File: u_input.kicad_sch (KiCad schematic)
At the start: 21 parts, among them U1 ${SIM.PARAMS}, U2 ${SIM.PARAMS}, U3 ${SIM.PARAMS}, U4 ${SIM.PARAMS}, U5 ${SIM.PARAMS}, U6 ${SIM.PARAMS}, U7 ${SIM.PARAMS}

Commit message: Before 10K resistors change
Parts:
- R1, R10, R11, R12, R13, R14, R2, R3, R4, R5, R6, R7, R8, R9: footprint (none) -> Resistor_SMD:R_1206_3216Metric_Pad1.30x1.75mm_HandSolder
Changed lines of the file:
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@@
 			)
 		)
-		(property "Footprint" ""
+		(property "Footprint" "Resistor_SMD:R_1206_3216Metric_Pad1.30x1.75mm_HandSolder"
 			(at 71.12 156.972 90)
 			(effects
@@
 			)
 		)
-		(property "Footprint" ""
+		(property "Footprint" "Resistor_SMD:R_1206_3216Metric_Pad1.30x1.75mm_HandSolder"
 			(at 73.66 355.092 90)
 			(effects
@@
 			)
 		)
-		(property "Footprint" ""
+		(property "Footprint" "Resistor_SMD:R_1206_3216Metric_Pad1.30x1.75mm_HandSolder"
 			(at 88.9 336.042 90)
 			(effects
@@
 			)
 		)
-		(property "Footprint" ""
+		(property "Footprint" "Resistor_SMD:R_1206_3216Metric_Pad1.30x1.75mm_HandSolder"
 			(at 71.12 70.612 90)
 			(effects
@@
 			)
 		)
-		(property "Footprint" ""
+		(property "Footprint" "Resistor_SMD:R_1206_3216Metric_Pad1.30x1.75mm_HandSolder"
 			(at 86.36 51.562 90)
 			(effects
@@
 			)
 		)
-		(property "Footprint" ""
+		(property "Footprint" "Resistor_SMD:R_1206_3216Metric_Pad1.30x1.75mm_HandSolder"
 			(at 86.36 137.922 90)
 			(effects
@@
 			)
 		)
-		(property "Footprint" ""
+		(property "Footprint" "Resistor_SMD:R_1206_3216Metric_Pad1.30x1.75mm_HandSolder"
 			(at 71.12 113.792 90)
 			(effects
@@
 			)
 		)
-		(property "Footprint" ""
+		(property "Footprint" "Resistor_SMD:R_1206_3216Metric_Pad1.30x1.75mm_HandSolder"
 			(at 88.9 290.322 90)
 			(effects
@@
 			)
 		)
-		(property "Footprint" ""
+		(property "Footprint" "Resistor_SMD:R_1206_3216Metric_Pad1.30x1.75mm_HandSolder"
 			(at 88.9 247.142 90)
 			(effects
@@
 			)
 		)
-		(property "Footprint" ""
+		(property "Footprint" "Resistor_SMD:R_1206_3216Metric_Pad1.30x1.75mm_HandSolder"
 			(at 88.9 203.962 90)
 			(effects
@@
 			)
 		)
-		(property "Footprint" ""
+		(property "Footprint" "Resistor_SMD:R_1206_3216Metric_Pad1.30x1.75mm_HandSolder"
 			(at 73.66 266.192 90)
 			(effects
@@
 			)
 		)
-		(property "Footprint" ""
+		(property "Footprint" "Resistor_SMD:R_1206_3216Metric_Pad1.30x1.75mm_HandSolder"
 			(at 86.36 94.742 90)
 			(effects
@@
 			)
 		)
-		(property "Footprint" ""
+		(property "Footprint" "Resistor_SMD:R_1206_3216Metric_Pad1.30x1.75mm_HandSolder"
 			(at 73.66 223.012 90)
 			(effects
@@
 			)
 		)
-		(property "Footprint" ""
+		(property "Footprint" "Resistor_SMD:R_1206_3216Metric_Pad1.30x1.75mm_HandSolder"
 			(at 73.66 309.372 90)
 			(effects

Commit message: Before capcitor update
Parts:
- R1, R10, R11, R12, R13, R14, R2, R3, R4, R5, R6, R7, R8, R9: value R -> 10k
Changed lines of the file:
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@@
 			)
 		)
-		(property "Value" "R"
+		(property "Value" "10k"
 			(at 71.12 154.94 90)
 			(effects
@@
 			)
 		)
-		(property "Value" "R"
+		(property "Value" "10k"
 			(at 73.66 353.06 90)
 			(effects
@@
 			)
 		)
-		(property "Value" "R"
+		(property "Value" "10k"
 			(at 88.9 334.01 90)
 			(effects
@@
 			)
 		)
-		(property "Value" "R"
+		(property "Value" "10k"
 			(at 71.12 68.58 90)
 			(effects
@@
 			)
 		)
-		(property "Value" "R"
+		(property "Value" "10k"
 			(at 86.36 49.53 90)
 			(effects
@@
 			)
 		)
-		(property "Value" "R"
+		(property "Value" "10k"
 			(at 86.36 135.89 90)
 			(effects
@@
 			)
 		)
-		(property "Value" "R"
+		(property "Value" "10k"
 			(at 71.12 111.76 90)
 			(effects
@@
 			)
 		)
-		(property "Value" "R"
+		(property "Value" "10k"
 			(at 88.9 288.29 90)
 			(effects
@@
 			)
 		)
-		(property "Value" "R"
+		(property "Value" "10k"
 			(at 88.9 245.11 90)
 			(effects
@@
 			)
 		)
-		(property "Value" "R"
+		(property "Value" "10k"
 			(at 88.9 201.93 90)
 			(effects
@@
 			)
 		)
-		(property "Value" "R"
+		(property "Value" "10k"
 			(at 73.66 264.16 90)
 			(effects
@@
 			)
 		)
-		(property "Value" "R"
+		(property "Value" "10k"
 			(at 86.36 92.71 90)
 			(effects
@@
 			)
 		)
-		(property "Value" "R"
+		(property "Value" "10k"
 			(at 73.66 220.98 90)
 			(effects
@@
 			)
 		)
-		(property "Value" "R"
+		(property "Value" "10k"
 			(at 73.66 307.34 90)
 			(effects

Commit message: Updated: power
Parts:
- removed U2: ${SIM.PARAMS}, symbol Simulation_SPICE:OPAMP
- added U43: TLV9061xDBV, Package_TO_SOT_SMD:SOT-23-5, symbol Amplifier_Operational:TLV9061xDBV
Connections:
- net -VCC is gone; now on net GND: U1.4 (V-), U3.4 (V-), U4.4 (V-), U5.4 (V-), U6.4 (V-), U7.4 (V-)
- net -Vu1: now also U43.1
- net GND: now also U43.2 (V-), U43.3 (+)
- net VCC: now also U43.5 (V+)
- net at R3.2, R4.1: now also U43.4 (-)

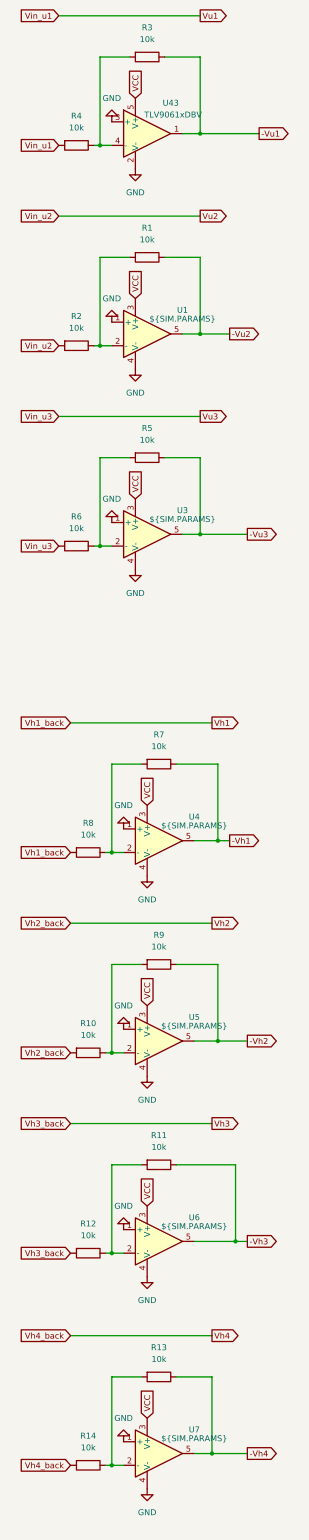
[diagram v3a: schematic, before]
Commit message: Updated: op amps
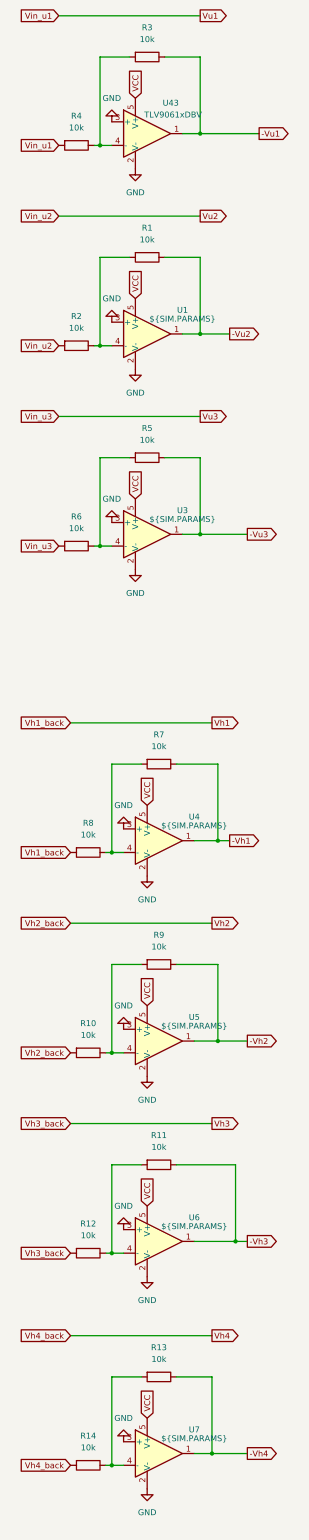
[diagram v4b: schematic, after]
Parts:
- U1, U3, U4, U5, U6, U7: footprint (none) -> Package_TO_SOT_SMD:SOT-23-5; symbol Simulation_SPICE:OPAMP -> Amplifier_Operational:TLV9061xDBV
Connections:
- net -Vh1: now also U4.1; no longer U4.5
- net -Vh2: now also U5.1; no longer U5.5
- net -Vh3: now also U6.1; no longer U6.5
- net -Vh4: now also U7.1; no longer U7.5
- net -Vu2: now also U1.1; no longer U1.5
- net -Vu3: now also U3.1; no longer U3.5
- net GND: now also U1.2 (V-), U1.3 (+), U3.2 (V-), U3.3 (+), U4.2 (V-), U4.3 (+), U5.2 (V-), U5.3 (+), U6.2 (V-), U6.3 (+), U7.2 (V-), U7.3 (+); no longer U1.1 (+), U1.4 (V-), U3.1 (+), U3.4 (V-), U4.1 (+), U4.4 (V-), U5.1 (+), U5.4 (V-), U6.1 (+), U6.4 (V-), U7.1 (+), U7.4 (V-)
- net VCC: now also U1.5 (V+), U3.5 (V+), U4.5 (V+), U5.5 (V+), U6.5 (V+), U7.5 (V+); no longer U1.3 (V+), U3.3 (V+), U4.3 (V+), U5.3 (V+), U6.3 (V+), U7.3 (V+)
- net at R5.2, R6.1: now also U3.4 (-); no longer U3.2 (-)
- net at R13.2, R14.1: now also U7.4 (-); no longer U7.2 (-)
- net at R1.2, R2.1: now also U1.4 (-); no longer U1.2 (-)
- net at R11.2, R12.1: now also U6.4 (-); no longer U6.2 (-)
- net at R10.1, R9.2: now also U5.4 (-); no longer U5.2 (-)
- net at R7.2, R8.1: now also U4.4 (-); no longer U4.2 (-)
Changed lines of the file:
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@@
 	)
 	(symbol
-		(lib_id "Simulation_SPICE:OPAMP")
+		(lib_id "Amplifier_Operational:TLV9061xDBV")
 		(at 86.36 113.03 0)
 		(unit 1)
@@
 			)
 		)
-		(property "Footprint" ""
-			(at 86.36 113.03 0)
-			(effects
-				(font
-					(size 1.27 1.27)
-				)
-				(hide yes)
-			)
-		)
-		(property "Datasheet" "https://ngspice.sourceforge.io/docs/ngspice-html-manual/manual.xhtml#sec__SUBCKT_Subcircuits"
-			(at 86.36 113.03 0)
-			(effects
-				(font
-					(size 1.27 1.27)
-				)
-				(hide yes)
-			)
-		)
-		(property "Description" "Operational amplifier, single"
+		(property "Footprint" "Package_TO_SOT_SMD:SOT-23-5"
+			(at 71.12 132.08 0)
+			(effects
+				(font
+					(size 1.27 1.27)
+				)
+				(justify left)
+				(hide yes)
+			)
+		)
+		(property "Datasheet" "https://www.ti.com/lit/ds/symlink/tlv9061.pdf"
+			(at 86.36 92.71 0)
+			(effects
+				(font
+					(size 1.27 1.27)
+				)
+				(hide yes)
+			)
+		)
+		(property "Description" "10-MHz, RRIO, CMOS Operational Amplifiers for Cost-Sensitive Systems, SOT-23-5"
 			(at 86.36 113.03 0)
 			(effects
@@
 	)
 	(symbol
-		(lib_id "Simulation_SPICE:OPAMP")
+		(lib_id "Amplifier_Operational:TLV9061xDBV")
 		(at 88.9 265.43 0)
 		(unit 1)
@@
 			)
 		)
-		(property "Footprint" ""
-			(at 88.9 265.43 0)
-			(effects
-				(font
-					(size 1.27 1.27)
-				)
-				(hide yes)
-			)
-		)
-		(property "Datasheet" "https://ngspice.sourceforge.io/docs/ngspice-html-manual/manual.xhtml#sec__SUBCKT_Subcircuits"
-			(at 88.9 265.43 0)
-			(effects
-				(font
-					(size 1.27 1.27)
-				)
-				(hide yes)
-			)
-		)
-		(property "Description" "Operational amplifier, single"
+		(property "Footprint" "Package_TO_SOT_SMD:SOT-23-5"
+			(at 73.66 284.48 0)
+			(effects
+				(font
+					(size 1.27 1.27)
+				)
+				(justify left)
+				(hide yes)
+			)
+		)
+		(property "Datasheet" "https://www.ti.com/lit/ds/symlink/tlv9061.pdf"
+			(at 88.9 245.11 0)
+			(effects
+				(font
+					(size 1.27 1.27)
+				)
+				(hide yes)
+			)
+		)
+		(property "Description" "10-MHz, RRIO, CMOS Operational Amplifiers for Cost-Sensitive Systems, SOT-23-5"
 			(at 88.9 265.43 0)
 			(effects
@@
 	)
 	(symbol
-		(lib_id "Simulation_SPICE:OPAMP")
+		(lib_id "Amplifier_Operational:TLV9061xDBV")
 		(at 88.9 354.33 0)
 		(unit 1)
@@
 			)
 		)
-		(property "Footprint" ""
-			(at 88.9 354.33 0)
-			(effects
-				(font
-					(size 1.27 1.27)
-				)
-				(hide yes)
-			)
-		)
-		(property "Datasheet" "https://ngspice.sourceforge.io/docs/ngspice-html-manual/manual.xhtml#sec__SUBCKT_Subcircuits"
-			(at 88.9 354.33 0)
-			(effects
-				(font
-					(size 1.27 1.27)
-				)
-				(hide yes)
-			)
-		)
-		(property "Description" "Operational amplifier, single"
+		(property "Footprint" "Package_TO_SOT_SMD:SOT-23-5"
+			(at 73.66 373.38 0)
+			(effects
+				(font
+					(size 1.27 1.27)
+				)
+				(justify left)
+				(hide yes)
+			)
+		)
+		(property "Datasheet" "https://www.ti.com/lit/ds/symlink/tlv9061.pdf"
+			(at 88.9 334.01 0)
+			(effects
+				(font
+					(size 1.27 1.27)
+				)
+				(hide yes)
+			)
+		)
+		(property "Description" "10-MHz, RRIO, CMOS Operational Amplifiers for Cost-Sensitive Systems, SOT-23-5"
 			(at 88.9 354.33 0)
 			(effects
@@
 	)
 	(symbol
-		(lib_id "Simulation_SPICE:OPAMP")
+		(lib_id "Amplifier_Operational:TLV9061xDBV")
 		(at 88.9 222.25 0)
 		(unit 1)
@@
 			)
 		)
-		(property "Footprint" ""
-			(at 88.9 222.25 0)
-			(effects
-				(font
-					(size 1.27 1.27)
-				)
-				(hide yes)
-			)
-		)
-		(property "Datasheet" "https://ngspice.sourceforge.io/docs/ngspice-html-manual/manual.xhtml#sec__SUBCKT_Subcircuits"
-			(at 88.9 222.25 0)
-			(effects
-				(font
-					(size 1.27 1.27)
-				)
-				(hide yes)
-			)
-		)
-		(property "Description" "Operational amplifier, single"
+		(property "Footprint" "Package_TO_SOT_SMD:SOT-23-5"
+			(at 73.66 241.3 0)
+			(effects
+				(font
+					(size 1.27 1.27)
+				)
+				(justify left)
+				(hide yes)
+			)
+		)
+		(property "Datasheet" "https://www.ti.com/lit/ds/symlink/tlv9061.pdf"
+			(at 88.9 201.93 0)
+			(effects
+				(font
+					(size 1.27 1.27)
+				)
+				(hide yes)
+			)
+		)
+		(property "Description" "10-MHz, RRIO, CMOS Operational Amplifiers for Cost-Sensitive Systems, SOT-23-5"
 			(at 88.9 222.25 0)
 			(effects
@@
 	)
 	(symbol
-		(lib_id "Simulation_SPICE:OPAMP")
+		(lib_id "Amplifier_Operational:TLV9061xDBV")
 		(at 88.9 308.61 0)
 		(unit 1)
@@
 			)
 		)
-		(property "Footprint" ""
-			(at 88.9 308.61 0)
-			(effects
-				(font
-					(size 1.27 1.27)
-				)
-				(hide yes)
-			)
-		)
-		(property "Datasheet" "https://ngspice.sourceforge.io/docs/ngspice-html-manual/manual.xhtml#sec__SUBCKT_Subcircuits"
-			(at 88.9 308.61 0)
-			(effects
-				(font
-					(size 1.27 1.27)
-				)
-				(hide yes)
-			)
-		)
-		(property "Description" "Operational amplifier, single"
+		(property "Footprint" "Package_TO_SOT_SMD:SOT-23-5"
+			(at 73.66 327.66 0)
+			(effects
+				(font
+					(size 1.27 1.27)
+				)
+				(justify left)
+				(hide yes)
+			)
+		)
+		(property "Datasheet" "https://www.ti.com/lit/ds/symlink/tlv9061.pdf"
+			(at 88.9 288.29 0)
+			(effects
+				(font
+					(size 1.27 1.27)
+				)
+				(hide yes)
+			)
+		)
+		(property "Description" "10-MHz, RRIO, CMOS Operational Amplifiers for Cost-Sensitive Systems, SOT-23-5"
 			(at 88.9 308.61 0)
 			(effects
@@
 	)
 	(symbol
-		(lib_id "Simulation_SPICE:OPAMP")
+		(lib_id "Amplifier_Operational:TLV9061xDBV")
 		(at 86.36 156.21 0)
 		(unit 1)
@@
 			)
 		)
-		(property "Footprint" ""
+		(property "Footprint" "Package_TO_SOT_SMD:SOT-23-5"
+			(at 71.12 175.26 0)
+			(effects
+				(font
+					(size 1.27 1.27)
+				)
+				(justify left)
+				(hide yes)
+			)
+		)
+		(property "Datasheet" "https://www.ti.com/lit/ds/symlink/tlv9061.pdf"
+			(at 86.36 135.89 0)
+			(effects
+				(font
+					(size 1.27 1.27)
+				)
+				(hide yes)
+			)
+		)
+		(property "Description" "10-MHz, RRIO, CMOS Operational Amplifiers for Cost-Sensitive Systems, SOT-23-5"
 			(at 86.36 156.21 0)
 			(effects
-				(font
-					(size 1.27 1.27)
-				)
-				(hide yes)
-			)
-		)
-		(property "Datasheet" "https://ngspice.sourceforge.io/docs/ngspice-html-manual/manual.xhtml#sec__SUBCKT_Subcircuits"
-			(at 86.36 156.21 0)
-			(effects
-				(font
-					(size 1.27 1.27)
-				)
-				(hide yes)
-			)
-		)
-		(property "Description" "Operational amplifier, single"
-			(at 86.36 156.21 0)
-			(effects

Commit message: Updated: pots
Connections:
- net GND: no longer U1.3 (+), U3.3 (+), U4.3 (+), U43.3 (+), U5.3 (+), U6.3 (+), U7.3 (+)
- new net VREF: U1.3 (+), U3.3 (+), U4.3 (+), U43.3 (+), U5.3 (+), U6.3 (+), U7.3 (+)
